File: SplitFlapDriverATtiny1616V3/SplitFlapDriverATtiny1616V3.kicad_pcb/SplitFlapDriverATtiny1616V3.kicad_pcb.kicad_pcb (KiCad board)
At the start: 2 copper layers, 30 x 60 mm, 25 parts, among them J1 UPDI Programming, J2 Conn_01x01_Pin, J3 Stepper Connector, J4 Hall Effect, J5 Conn_01x05_Pin, J6 Conn_01x01_Pin, J7 Conn_01x01_Pin, J8 Conn_01x01_Pin, U1 ATtiny1616-MNR, U2 ULN2003ADR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

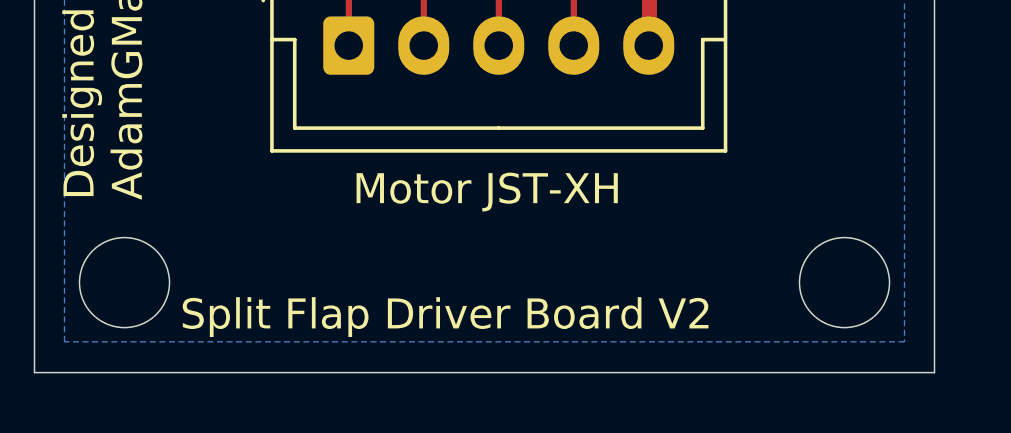
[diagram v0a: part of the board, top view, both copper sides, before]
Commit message: Updated V3 board screenprint to include "V3"
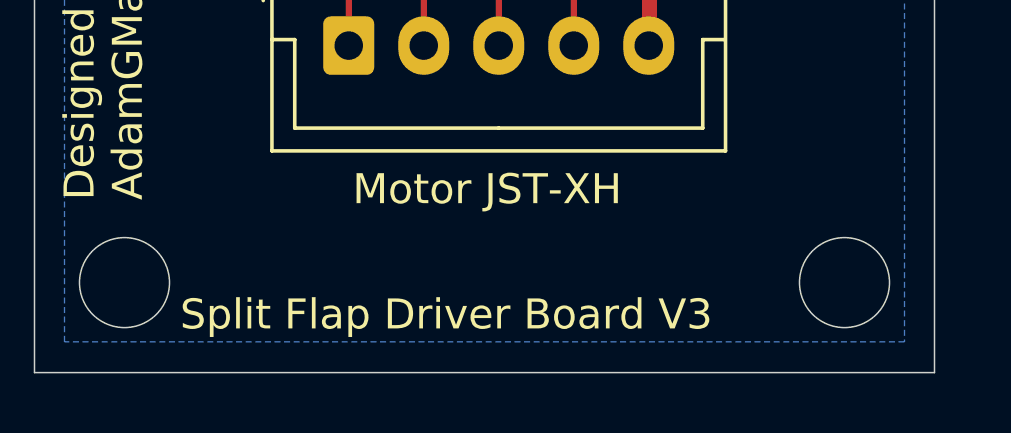
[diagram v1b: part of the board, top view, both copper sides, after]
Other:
- board text added: "Split Flap Driver Board V3"
- board text removed: "Split Flap Driver Board V2"
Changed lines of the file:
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@@
 		)
 	)
-	(gr_text "Split Flap Driver Board V2"
+	(gr_text "Split Flap Driver Board V3"
 		(at 124.85 138.65 0)
 		(layer "F.SilkS")
